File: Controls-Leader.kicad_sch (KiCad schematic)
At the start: 48 parts, among them J1 ExtraADCs, J13 UART_TP, J15 Conn_02x03_Odd_Even, J2 UART_TP, J25 UART_TP, J3 ExtraGPIO_Conn, J8 SWD, SW10 RESET, U7 STM32F413RHTx, Y1 Crystal

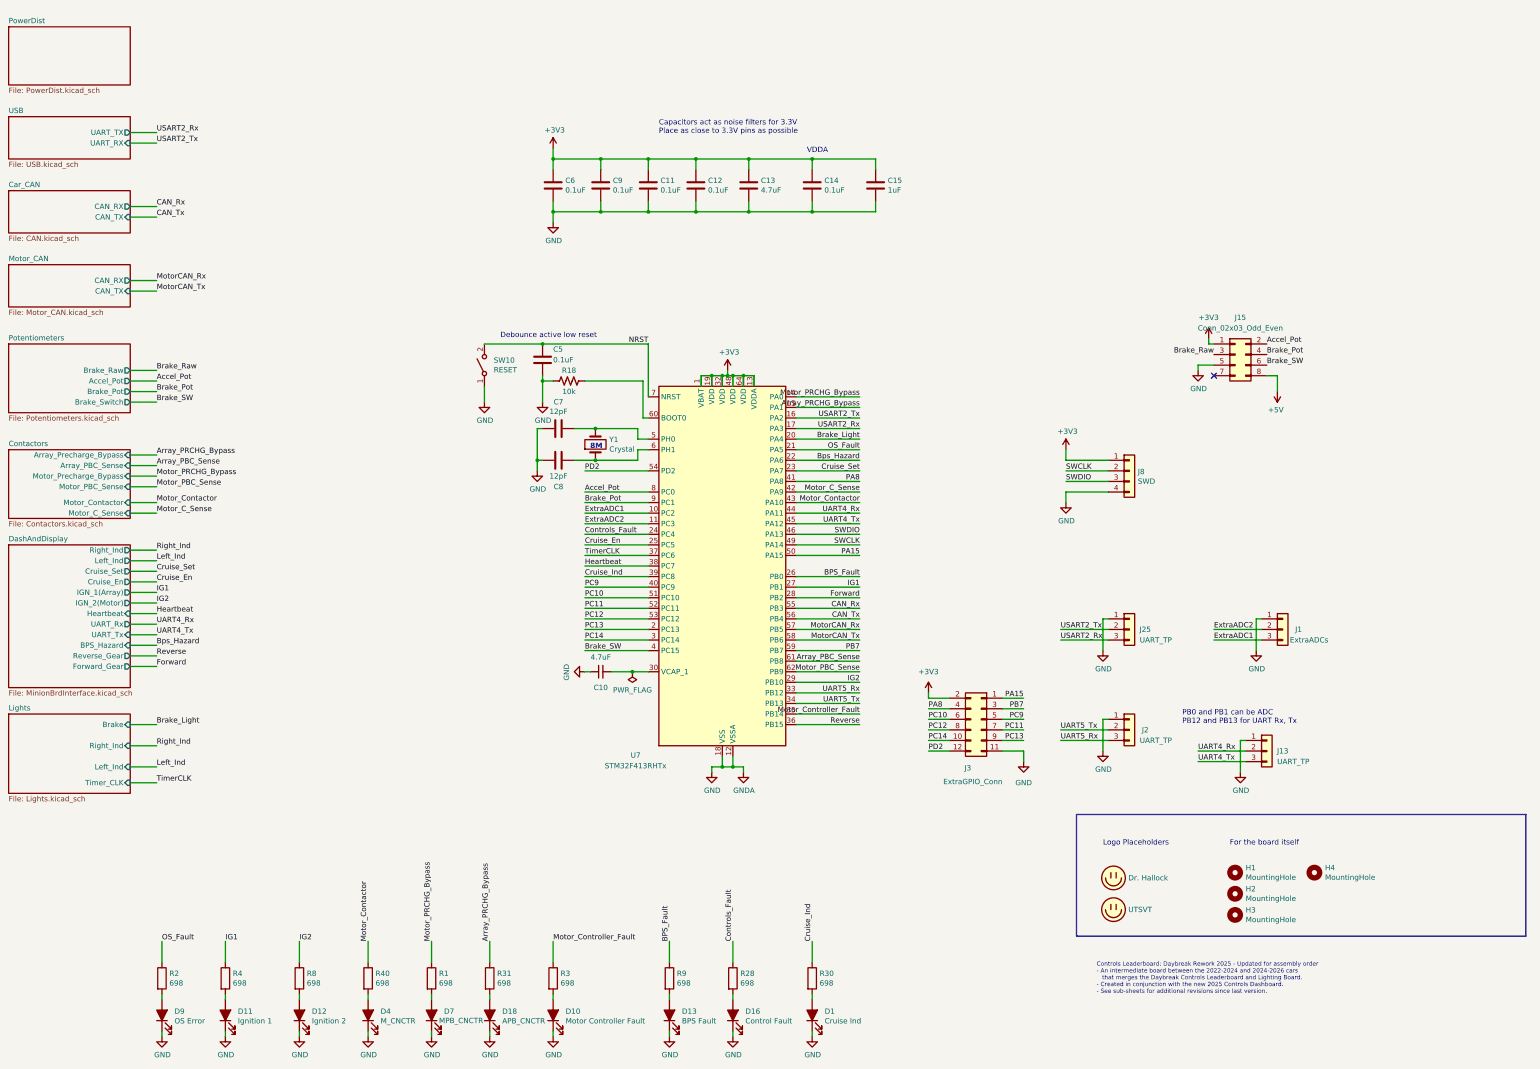
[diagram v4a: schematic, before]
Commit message: Changed lights to direct drive instead of timer_CLK optoisolator stuff.
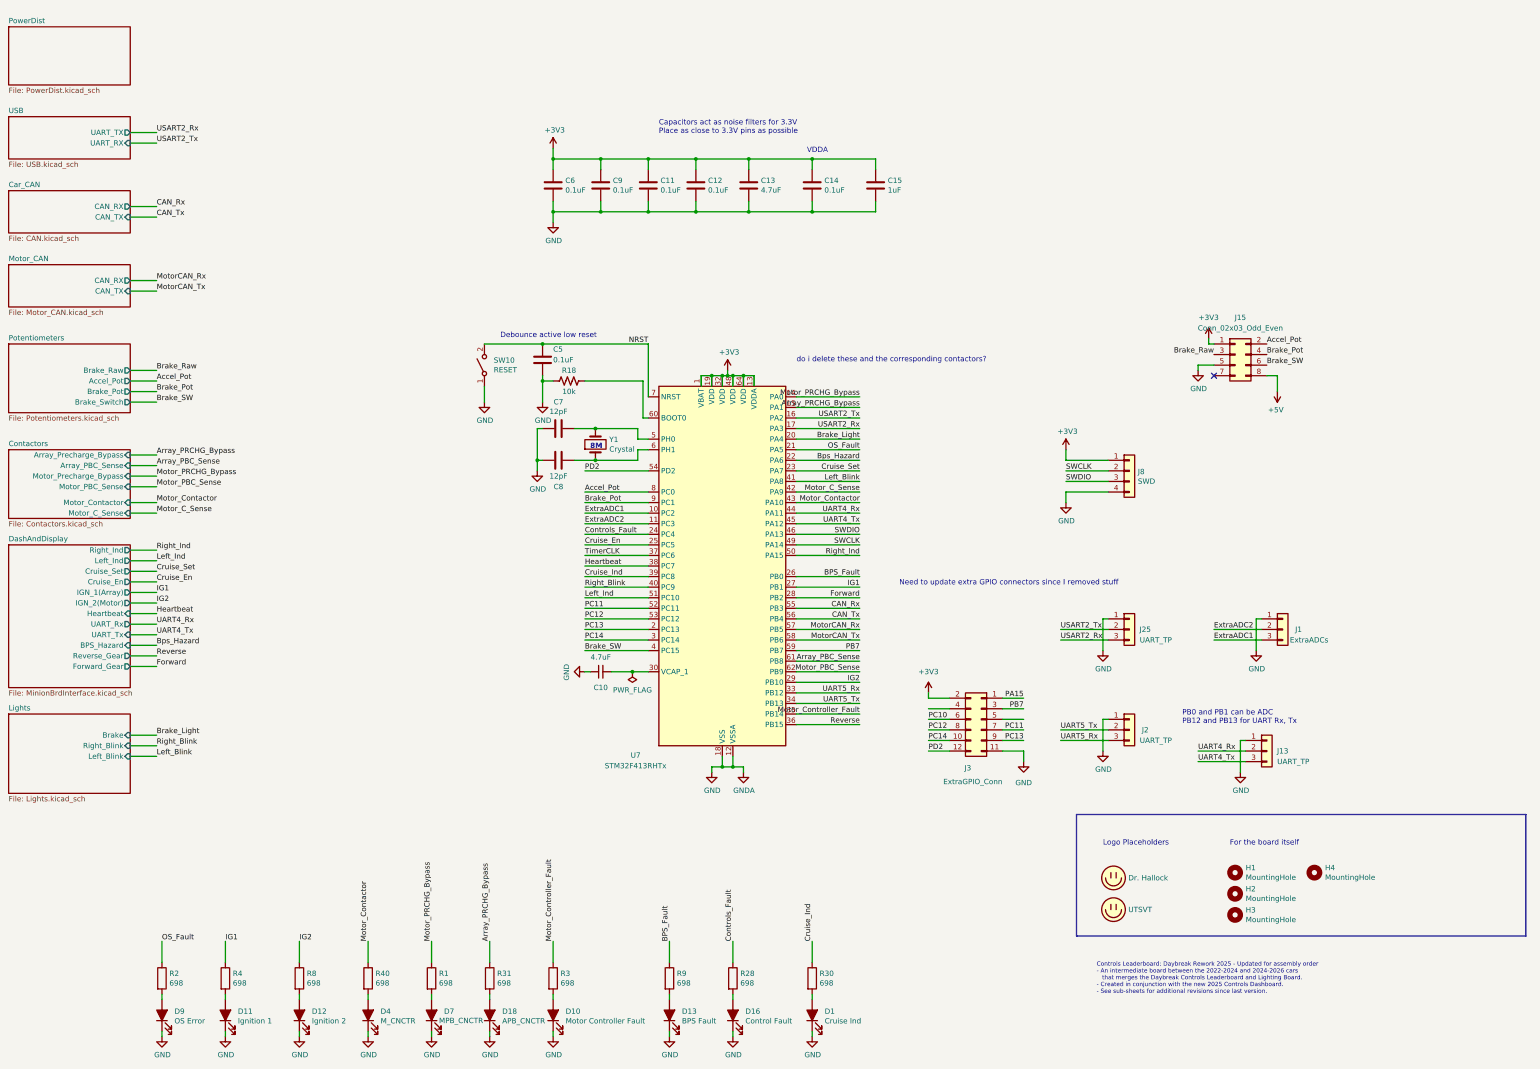
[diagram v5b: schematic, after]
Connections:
- net Left_Ind: now also U7.51 (PC10)
- net PA15: no longer U7.50 (PA15)
- net PC10: no longer U7.51 (PC10)
- net Right_Ind: now also U7.50 (PA15)
- net PA8: no longer names the net of J3.4 (Pin_4)
- net PA8: no longer U7.41 (PA8)
- net PC9: no longer names the net of J3.5 (Pin_5)
- net PC9: no longer U7.40 (PC9)
- new net Left_Blink: U7.41 (PA8)
- new net Right_Blink: U7.40 (PC9)
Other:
- sheet Lights ports: added Left_Blink, Right_Blink; removed Left_Ind, Right_Ind, Timer_CLK
- note added: "Need to update extra GPIO connectors since I removed stuff"
- note added: "do i delete these and the corresponding contactors?"
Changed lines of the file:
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@@
 	(wire
 		(pts
-			(xy 68.58 196.85) (xy 74.93 196.85)
+			(xy 68.58 199.39) (xy 74.93 199.39)
 		)
 		(stroke
@@
 	(wire
 		(pts
-			(xy 68.58 210.82) (xy 74.93 210.82)
-		)
-		(stroke
-			(width 0)
-			(type default)
-		)
-	)
-	(wire
-		(pts
 			(xy 243.84 125.73) (xy 228.6 125.73)
 		)
@@
 	(wire
 		(pts
-			(xy 68.58 207.01) (xy 74.93 207.01)
+			(xy 68.58 204.47) (xy 74.93 204.47)
 		)
 		(stroke
@@
 		)
 	)
+	(text "Need to update extra GPIO connectors since I removed stuff\n"
+		(exclude_from_sim no)
+		(at 279.654 162.814 0)
+		(effects
+			(font
+				(size 1.27 1.27)
+				(color 255 14 125 1)
+			)
+		)
+	)
 	(text "PB0 and PB1 can be ADC\nPB12 and PB13 for UART Rx, Tx\n"
 		(exclude_from_sim no)
@@
 		)
 	)
+	(text "do i delete these and the corresponding contactors?"
+		(exclude_from_sim no)
+		(at 251.46 109.22 0)
+		(effects
+			(font
+				(size 1.27 1.27)
+				(color 156 87 255 1)
+			)
+		)
+	)
 	(text "Capacitors act as noise filters for 3.3V\nPlace as close to 3.3V pins as possible\n\n"
 		(exclude_from_sim no)
@@
 		)
 	)
+	(label "Right_Blink"
+		(at 177.8 163.83 0)
+		(fields_autoplaced yes)
+		(effects
+			(font
+				(size 1.27 1.27)
+			)
+			(justify left bottom)
+		)
+	)
 	(label "PC13"
 		(at 177.8 173.99 0)
@@
 		)
 	)
-	(label "PC9"
-		(at 177.8 163.83 0)
-		(fields_autoplaced yes)
-		(effects
-			(font
-				(size 1.27 1.27)
-			)
-			(justify left bottom)
-		)
-	)
 	(label "IG2"
 		(at 74.93 167.64 0)
@@
 		)
 	)
-	(label "PC9"
-		(at 283.21 195.58 180)
-		(fields_autoplaced yes)
-		(effects
-			(font
-				(size 1.27 1.27)
-			)
-			(justify right bottom)
-		)
-	)
 	(label "ExtraADC2"
 		(at 328.93 173.99 0)
@@
 		)
 	)
-	(label "Right_Ind"
+	(label "Right_Blink"
 		(at 74.93 201.93 0)
 		(fields_autoplaced yes)
@@
 		)
 	)
-	(label "PC10"
-		(at 177.8 166.37 0)
-		(fields_autoplaced yes)
-		(effects
-			(font
-				(size 1.27 1.27)
-			)
-			(justify left bottom)
-		)
-	)
 	(label "Motor_PRCHG_Bypass"
 		(at 74.93 137.16 0)
@@
 		)
 	)
-	(label "PA8"
-		(at 243.84 138.43 180)
-		(fields_autoplaced yes)
-		(effects
-			(font
-				(size 1.27 1.27)
-			)
-			(justify right bottom)
-		)
-	)
 	(label "Cruise_Set"
 		(at 74.93 160.02 0)
@@
 	)
 	(label "Brake_Light"
-		(at 74.93 196.85 0)
+		(at 74.93 199.39 0)
 		(fields_autoplaced yes)
 		(effects
@@
 		)
 	)
-	(label "Left_Ind"
-		(at 74.93 207.01 0)
+	(label "Left_Blink"
+		(at 74.93 204.47 0)
 		(fields_autoplaced yes)
 		(effects
@@
 		)
 	)
+	(label "Left_Blink"
+		(at 243.84 138.43 180)
+		(fields_autoplaced yes)
+		(effects
+			(font
+				(size 1.27 1.27)
+			)
+			(justify right bottom)
+		)
+	)
 	(label "Motor_PRCHG_Bypass"
 		(at 243.84 118.11 180)
@@
 	)
 	(label "Motor_Controller_Fault"
-		(at 170.18 248.92 0)
+		(at 170.18 248.92 90)
 		(fields_autoplaced yes)
 		(effects
@@
 		)
 	)
+	(label "Left_Ind"
+		(at 177.8 166.37 0)
+		(fields_autoplaced yes)
+		(effects
+			(font
+				(size 1.27 1.27)
+			)
+			(justify left bottom)
+		)
+	)
 	(label "UART5_Tx"
 		(at 243.84 191.77 180)
@@
 		)
 	)
-	(label "TimerCLK"
-		(at 74.93 210.82 0)
-		(fields_autoplaced yes)
-		(effects
-			(font
-				(size 1.27 1.27)
-			)
-			(justify left bottom)
-		)
-	)
 	(label "UART5_Tx"
 		(at 292.1 198.12 0)
@@
 		)
 	)
-	(label "PA15"
-		(at 243.84 156.21 180)
-		(fields_autoplaced yes)
-		(effects
-			(font
-				(size 1.27 1.27)
-			)
-			(justify right bottom)
-		)
-	)
 	(label "PC14"
 		(at 177.8 176.53 0)
@@
 		)
 	)
-	(label "PA8"
-		(at 260.35 193.04 0)
+	(label "Right_Ind"
+		(at 243.84 156.21 180)
 		(fields_autoplaced yes)
 		(effects
@@
 				(size 1.27 1.27)
 			)
-			(justify left bottom)
+			(justify right bottom)
 		)
 	)
@@
 		)
 		(pin "Brake" input
-			(at 68.58 196.85 0)
+			(at 68.58 199.39 0)
 			(effects
 				(font
@@
 			)
 		)
-		(pin "Right_Ind" input
-			(at 68.58 201.93 0)
+		(pin "Left_Blink" input
+			(at 68.58 204.47 0)
 			(effects
 				(font
@@
 			)
 		)
-		(pin "Left_Ind" input
-			(at 68.58 207.01 0)
-			(effects
-				(font
-					(size 1.27 1.27)
-				)
-				(justify right)
-			)
-		)
-		(pin "Timer_CLK" input
-			(at 68.58 210.82 0)
+		(pin "Right_Blink" input
+			(at 68.58 201.93 0)
 			(effects
 				(font

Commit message: Removed precharge contactor stuff, made accel 5V instead of 3, removed op amp for brake.
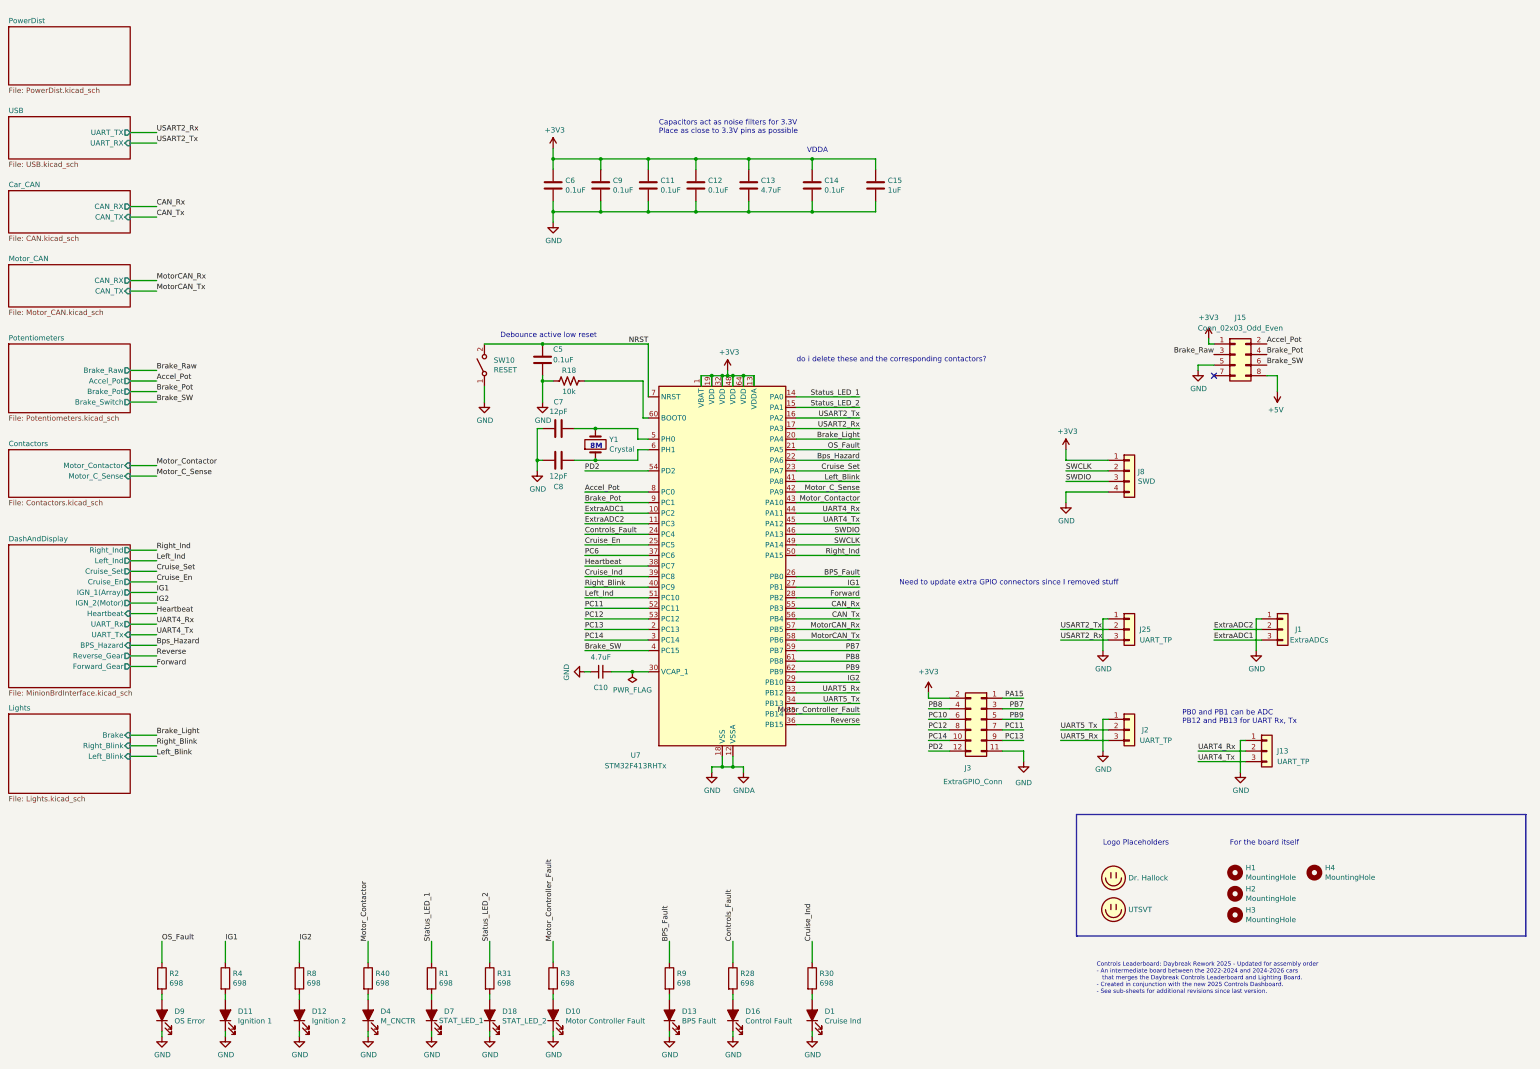
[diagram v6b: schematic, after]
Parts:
- D18: value APB_CNCTR -> STAT_LED_2
- D7: value MPB_CNCTR -> STAT_LED_1
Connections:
- net Array_PBC_Sense is gone; now on net PB8: U7.61 (PB8)
- net Motor_PBC_Sense is gone; now on net PB9: U7.62 (PB9)
- net PB8: now reaches J3.4 (Pin_4)
- net PB9: now reaches J3.5 (Pin_5)
- net Array_PRCHG_Bypass renamed Status_LED_2
- net Motor_PRCHG_Bypass renamed Status_LED_1
- net TimerCLK renamed PC6
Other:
- sheet Contactors ports: added none; removed Array_PBC_Sense, Array_Precharge_Bypass, Motor_PBC_Sense, Motor_Precharge_Bypass
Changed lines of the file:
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@@
 	(wire
 		(pts
-			(xy 68.58 139.7) (xy 74.93 139.7)
-		)
-		(stroke
-			(width 0)
-			(type default)
-		)
-	)
-	(wire
-		(pts
 			(xy 303.53 176.53) (xy 292.1 176.53)
 		)
@@
 	(wire
 		(pts
-			(xy 68.58 143.51) (xy 74.93 143.51)
+			(xy 68.58 134.62) (xy 74.93 134.62)
 		)
 		(stroke
@@
 	(wire
 		(pts
-			(xy 68.58 132.08) (xy 74.93 132.08)
-		)
-		(stroke
-			(width 0)
-			(type default)
-		)
-	)
-	(wire
-		(pts
 			(xy 68.58 165.1) (xy 74.93 165.1)
 		)
@@
 	(wire
 		(pts
-			(xy 68.58 146.05) (xy 74.93 146.05)
+			(xy 68.58 137.16) (xy 74.93 137.16)
 		)
 		(stroke
@@
 	(wire
 		(pts
-			(xy 68.58 134.62) (xy 74.93 134.62)
-		)
-		(stroke
-			(width 0)
-			(type default)
-		)
-	)
-	(wire
-		(pts
 			(xy 217.17 60.96) (xy 232.41 60.96)
 		)
@@
 	(wire
 		(pts
-			(xy 68.58 137.16) (xy 74.93 137.16)
-		)
-		(stroke
-			(width 0)
-			(type default)
-		)
-	)
-	(wire
-		(pts
 			(xy 213.36 204.47) (xy 213.36 207.01)
 		)
@@
 		)
 	)
-	(label "Array_PRCHG_Bypass"
+	(label "Status_LED_2"
 		(at 154.94 248.92 90)
 		(fields_autoplaced yes)
@@
 		)
 	)
-	(label "PC14"
-		(at 260.35 200.66 0)
+	(label "PB9"
+		(at 283.21 195.58 180)
 		(fields_autoplaced yes)
 		(effects
@@
 				(size 1.27 1.27)
 			)
-			(justify left bottom)
+			(justify right bottom)
 		)
 	)
-	(label "TimerCLK"
-		(at 177.8 156.21 0)
+	(label "PC14"
+		(at 260.35 200.66 0)
 		(fields_autoplaced yes)
 		(effects
@@
 		)
 	)
-	(label "Array_PBC_Sense"
-		(at 74.93 134.62 0)
-		(fields_autoplaced yes)
-		(effects
-			(font
-				(size 1.27 1.27)
-			)
-			(justify left bottom)
-		)
-	)
 	(label "CAN_Tx"
 		(at 74.93 74.93 0)
@@
 		)
 	)
-	(label "Array_PBC_Sense"
-		(at 243.84 181.61 180)
-		(fields_autoplaced yes)
-		(effects
-			(font
-				(size 1.27 1.27)
-			)
-			(justify right bottom)
-		)
-	)
 	(label "Brake_Pot"
 		(at 177.8 143.51 0)
@@
 		)
 	)
-	(label "Array_PRCHG_Bypass"
+	(label "Status_LED_2"
 		(at 243.84 120.65 180)
 		(fields_autoplaced yes)
@@
 		)
 	)
+	(label "PB8"
+		(at 243.84 181.61 180)
+		(fields_autoplaced yes)
+		(effects
+			(font
+				(size 1.27 1.27)
+			)
+			(justify right bottom)
+		)
+	)
 	(label "IG1"
 		(at 91.44 248.92 0)
@@
 		)
 	)
+	(label "PB8"
+		(at 260.35 193.04 0)
+		(fields_autoplaced yes)
+		(effects
+			(font
+				(size 1.27 1.27)
+			)
+			(justify left bottom)
+		)
+	)
 	(label "MotorCAN_Tx"
 		(at 243.84 176.53 180)
@@
 		)
 	)
-	(label "Motor_PRCHG_Bypass"
-		(at 74.93 137.16 0)
+	(label "Status_LED_1"
+		(at 140.97 248.92 90)
 		(fields_autoplaced yes)
 		(effects
@@
 		)
 	)
-	(label "Motor_PRCHG_Bypass"
-		(at 140.97 248.92 90)
+	(label "PC6"
+		(at 177.8 156.21 0)
 		(fields_autoplaced yes)
 		(effects
@@
 		)
 	)
-	(label "Motor_PRCHG_Bypass"
+	(label "Status_LED_1"
 		(at 243.84 118.11 180)
 		(fields_autoplaced yes)
@@
 		)
 	)
+	(label "PB9"
+		(at 243.84 184.15 180)
+		(fields_autoplaced yes)
+		(effects
+			(font
+				(size 1.27 1.27)
+			)
+			(justify right bottom)
+		)
+	)
 	(label "Left_Ind"
 		(at 177.8 166.37 0)
@@
 		)
 	)
-	(label "Motor_PBC_Sense"
-		(at 74.93 139.7 0)
-		(fields_autoplaced yes)
-		(effects
-			(font
-				(size 1.27 1.27)
-			)
-			(justify left bottom)
-		)
-	)
 	(label "MotorCAN_Rx"
 		(at 74.93 90.17 0)
@@
 	)
 	(label "Motor_Contactor"
-		(at 74.93 143.51 0)
+		(at 74.93 134.62 0)
 		(fields_autoplaced yes)
 		(effects
@@
 		)
 	)
-	(label "Motor_PBC_Sense"
-		(at 243.84 184.15 180)
-		(fields_autoplaced yes)
-		(effects
-			(font
-				(size 1.27 1.27)
-			)
-			(justify right bottom)
-		)
-	)
 	(label "PC11"
 		(at 177.8 168.91 0)
@@
 		)
 	)
-	(label "Array_PRCHG_Bypass"
-		(at 74.93 132.08 0)
-		(fields_autoplaced yes)
-		(effects
-			(font
-				(size 1.27 1.27)
-			)
-			(justify left bottom)
-		)
-	)
 	(label "Motor_C_Sense"
-		(at 74.93 146.05 0)
+		(at 74.93 137.16 0)
 		(fields_autoplaced yes)
 		(effects
@@
 			)
 		)
-		(property "Value" "APB_CNCTR"
+		(property "Value" "STAT_LED_2"
 			(at 157.9372 268.0462 90)
 			(effects
@@
 			)
 		)
-		(property "Value" "MPB_CNCTR"
+		(property "Value" "STAT_LED_1"
 			(at 142.748 267.97 90)
 			(effects
@@
 	(sheet
 		(at 39.37 130.81)
-		(size 29.21 16.51)
+		(size 29.21 11.43)
 		(fields_autoplaced yes)
 		(stroke
@@
 		)
 		(property "Sheetfile" "Contactors.kicad_sch"
-			(at 39.37 147.9046 0)
+			(at 39.37 142.8246 0)
 			(effects
 				(font
@@
 			)
 		)
-		(pin "Array_PBC_Sense" input
-			(at 68.58 134.62 0)
-			(effects
-				(font
-					(size 1.27 1.27)
-				)
-				(justify right)
-			)
-		)
 		(pin "Motor_C_Sense" input
-			(at 68.58 146.05 0)
-			(effects
-				(font
-					(size 1.27 1.27)
-				)
-				(justify right)
-			)
-		)
-		(pin "Array_Precharge_Bypass" input
-			(at 68.58 132.08 0)
+			(at 68.58 137.16 0)
 			(effects
 				(font
@@
 		)
 		(pin "Motor_Contactor" input
-			(at 68.58 143.51 0)
-			(effects
-				(font
-					(size 1.27 1.27)
-				)
-				(justify right)
-			)
-		)
-		(pin "Motor_PBC_Sense" input
-			(at 68.58 139.7 0)
-			(effects
-				(font
-					(size 1.27 1.27)
-				)
-				(justify right)
-			)
-		)
-		(pin "Motor_Precharge_Bypass" input
-			(at 68.58 137.16 0)
+			(at 68.58 134.62 0)
 			(effects
 				(font

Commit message: Layout and routing.
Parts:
- added J10: Dashboard_TPs, UTSVT_Connectors:Molex_MicroFit3.0_2x6xP3.00mm_PolarizingPeg_Vertical, symbol Connector_Generic:Conn_02x06_Top_Bottom
- J15: value Conn_02x03_Odd_Even -> Pot_TPs; footprint Connector_PinHeader_2.54mm:PinHeader_2x04_P2.54mm_Vertical -> Connector_PinHeader_2.54mm:PinHeader_2x03_P2.54mm_Vertical; symbol Connector_Generic:Conn_02x04_Odd_Even -> Connector_Generic:Conn_02x03_Odd_Even
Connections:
- net Brake_Raw is gone; now on net +5V: J15.3 (Pin_3)
- net PC6 is gone; now on net Brake_Light: U7.37 (PC6)
- net +5V: no longer J15.8 (Pin_8)
- net Bps_Hazard: now also J10.9 (Pin_9)
- net Brake_Light: no longer U7.20 (PA4)
- net Cruise_En: now also J10.3 (Pin_3)
- net Cruise_Set: now also J10.4 (Pin_4)
- net Forward: now also J10.7 (Pin_7)
- net Heartbeat: now also J10.12 (Pin_12)
- net IG1: now also J10.2 (Pin_2)
- net IG2: now also J10.1 (Pin_1)
- net Left_Ind: now also J10.5 (Pin_5)
- net Reverse: now also J10.8 (Pin_8)
- net Right_Ind: now also J10.6 (Pin_6)
- net UART4_Rx: now also J10.11 (Pin_11)
- net UART4_Tx: now also J10.10 (Pin_10)
- net PA15 renamed PA4
- net PA4: now also U7.20 (PA4)
- net PC10: no longer names the net of J3.6 (Pin_6)
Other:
- sheet Potentiometers ports: added none; removed Brake_Raw
- note removed: "Need to update extra GPIO connectors since I removed stuff"
- note removed: "do i delete these and the corresponding contactors?"
